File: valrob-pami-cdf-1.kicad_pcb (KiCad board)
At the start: 4 copper layers, 58 x 50 mm, 138 parts, among them J1 Conn_01x04, J2 USB_C_Receptacle_USB2.0_14P, J3 Conn_01x02, J4 Conn_01x04_Pin, J5 Conn_01x06, M1 Motor_Servo, M2 Stepper_Motor_bipolar, M3 Stepper_Motor_bipolar, Q1 Q_NMOS, Q2 Q_NMOS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

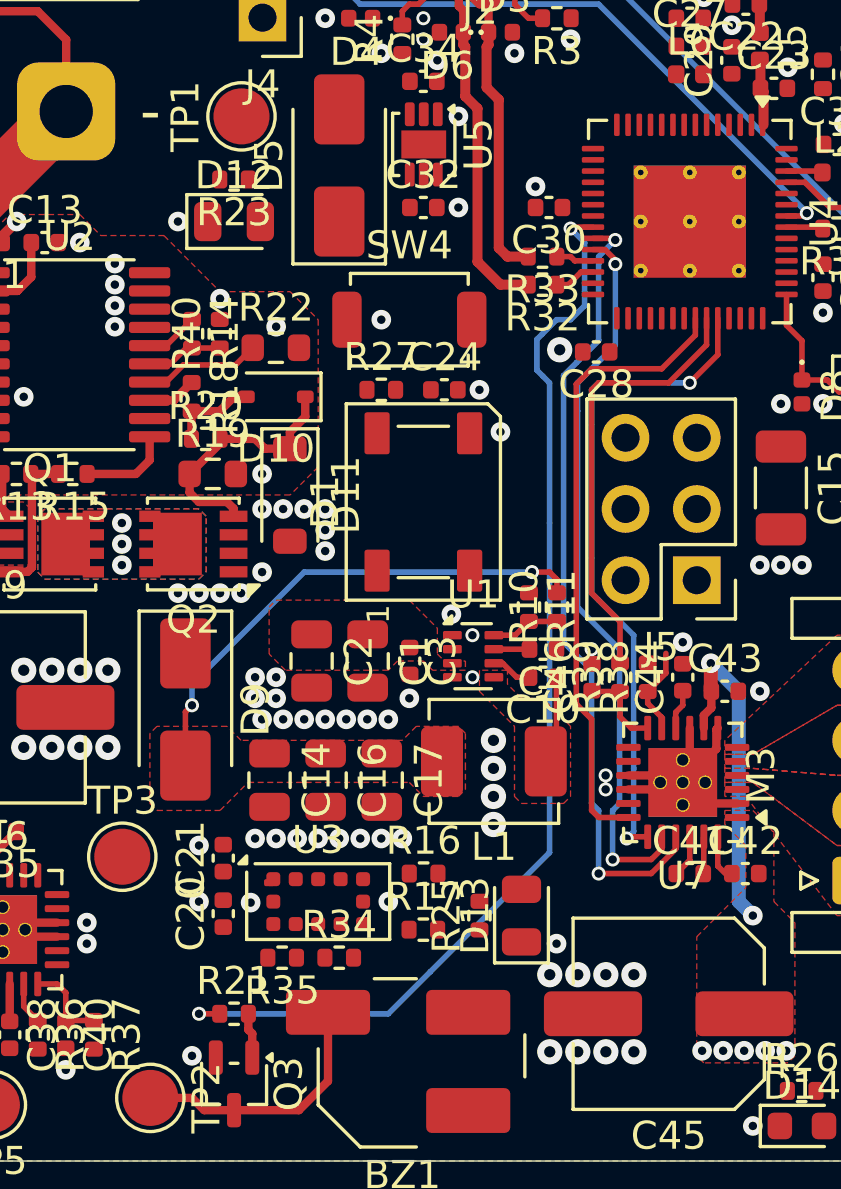
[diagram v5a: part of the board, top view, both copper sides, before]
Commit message: pcb: add tof sensor routing
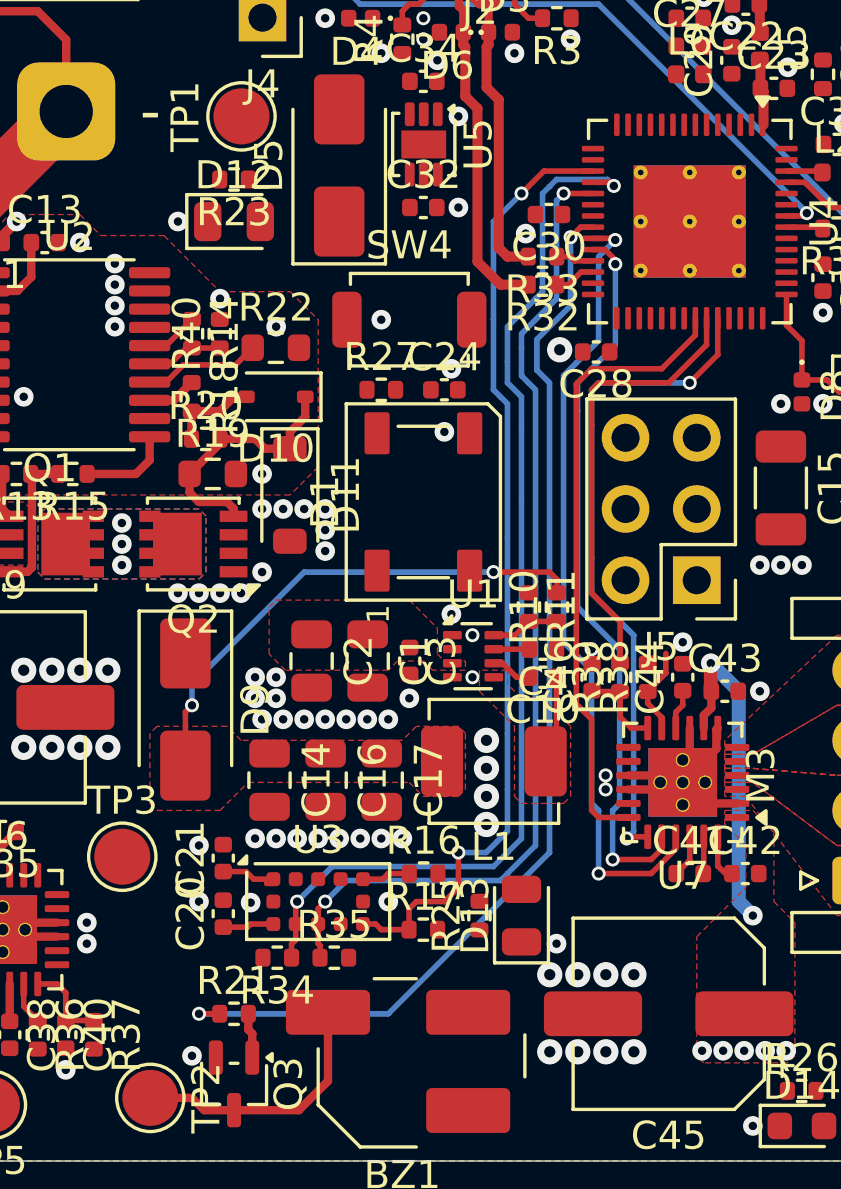
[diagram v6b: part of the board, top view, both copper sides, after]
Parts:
- moved R34 2.21 mm to (154.0, 115.8), turned to 180 degrees
- moved R35 1.86 mm to (156.1, 115.8), turned to 0 degrees
- moved C30 0.25 mm to (163.7, 89.2)
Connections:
- R17 pad 1: Net-(U3-GPIO1) -> /TOF_INT
- R34 pad 1: /SDA -> /SCL
- R34 pad 2: unconnected-(R34-Pad2) -> +3V3
- R35 pad 1: /SCL -> /SDA
- U3 pad 7: Net-(U3-GPIO1) -> /TOF_INT
- U4 pad 17: unconnected-(U4-GPIO12/ADC2_CH1-Pad17) -> /TOF_INT
- U4 pad 18: unconnected-(U4-GPIO13/ADC2_CH2-Pad18) -> /SCL
- U4 pad 19: unconnected-(U4-GPIO14/ADC2_CH3-Pad19) -> /SDA
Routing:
- net /SCL: track 0.00 -> 38.5 mm, vias 0 -> 2
- net /SDA: track 0.00 -> 35.6 mm, vias 0 -> 2
- net /TOF_INT: track 0.00 -> 34.1 mm, vias 0 -> 2
- net +3V3: track 0.00 -> 3.73 mm
- net Net-(U3-XSHUT): track 0.00 -> 1.73 mm
- net /BUZZER: track 40.1 -> 39.2 mm

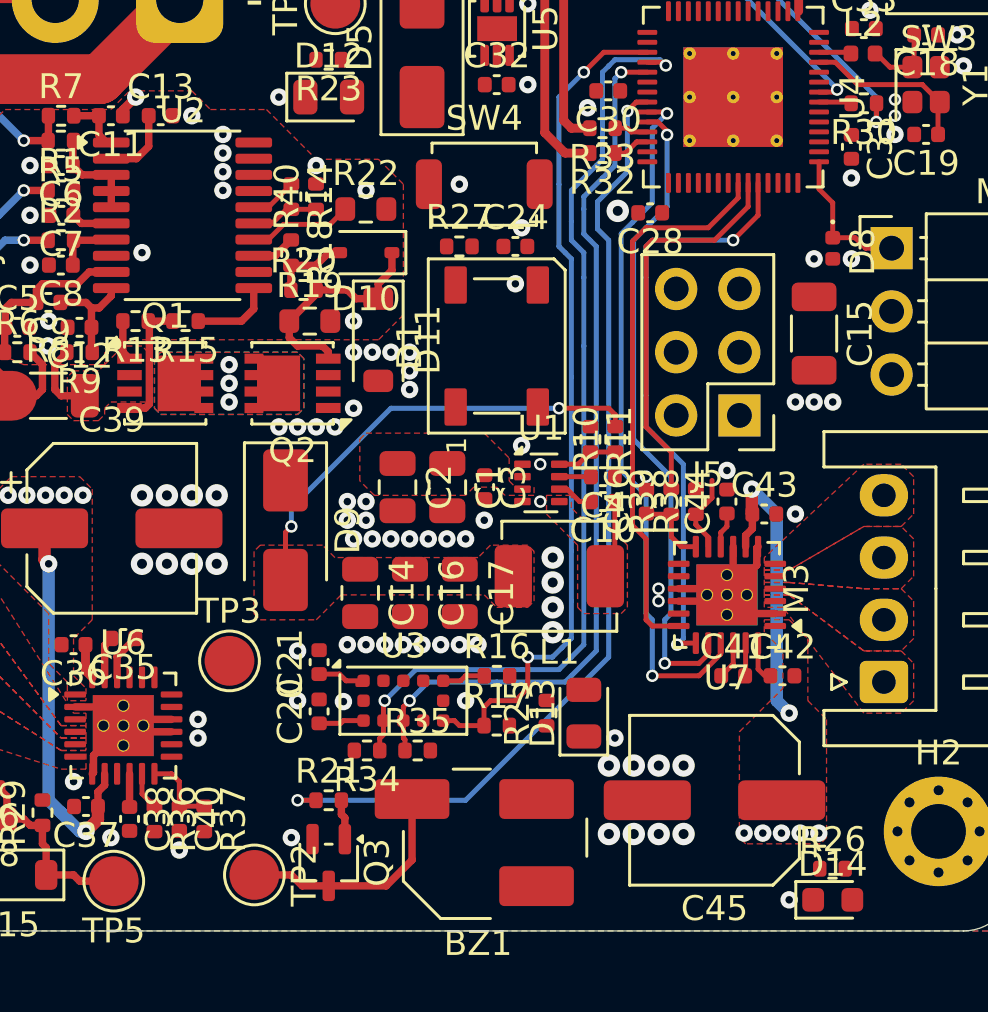
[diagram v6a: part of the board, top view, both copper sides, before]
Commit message: pcb: add missing stepper drv fault 2 connection
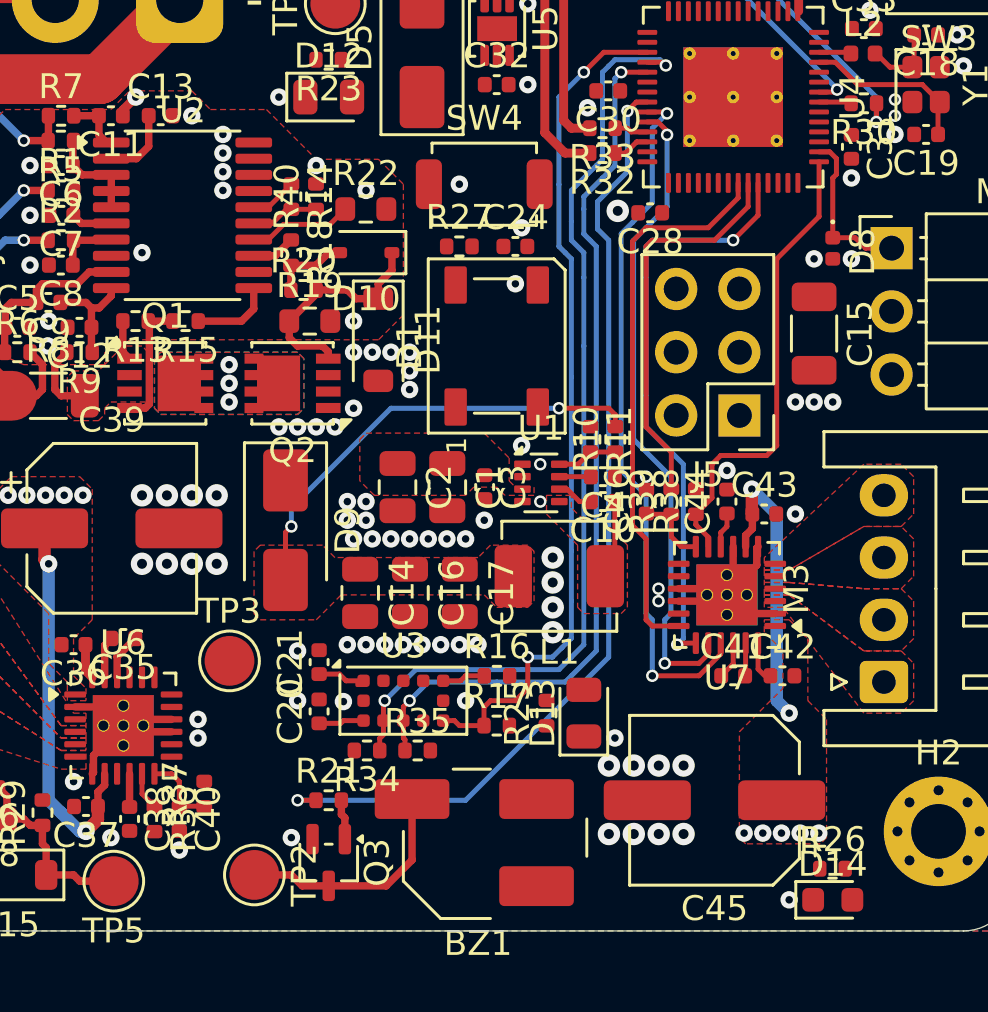
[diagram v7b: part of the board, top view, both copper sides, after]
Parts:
- moved R37 1.00 mm to (147.5, 117.5), turned to 90 degrees
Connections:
- U4 pad 43: /SERVO1 -> /~{FAULT_2}
- U4 pad 44: unconnected-(U4-MTCK/JTAG/GPIO39-Pad44) -> /SERVO1
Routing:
- net /~{FAULT_2}: track 3.14 -> 18.8 mm
- net /SERVO1: track 5.82 -> 6.59 mm

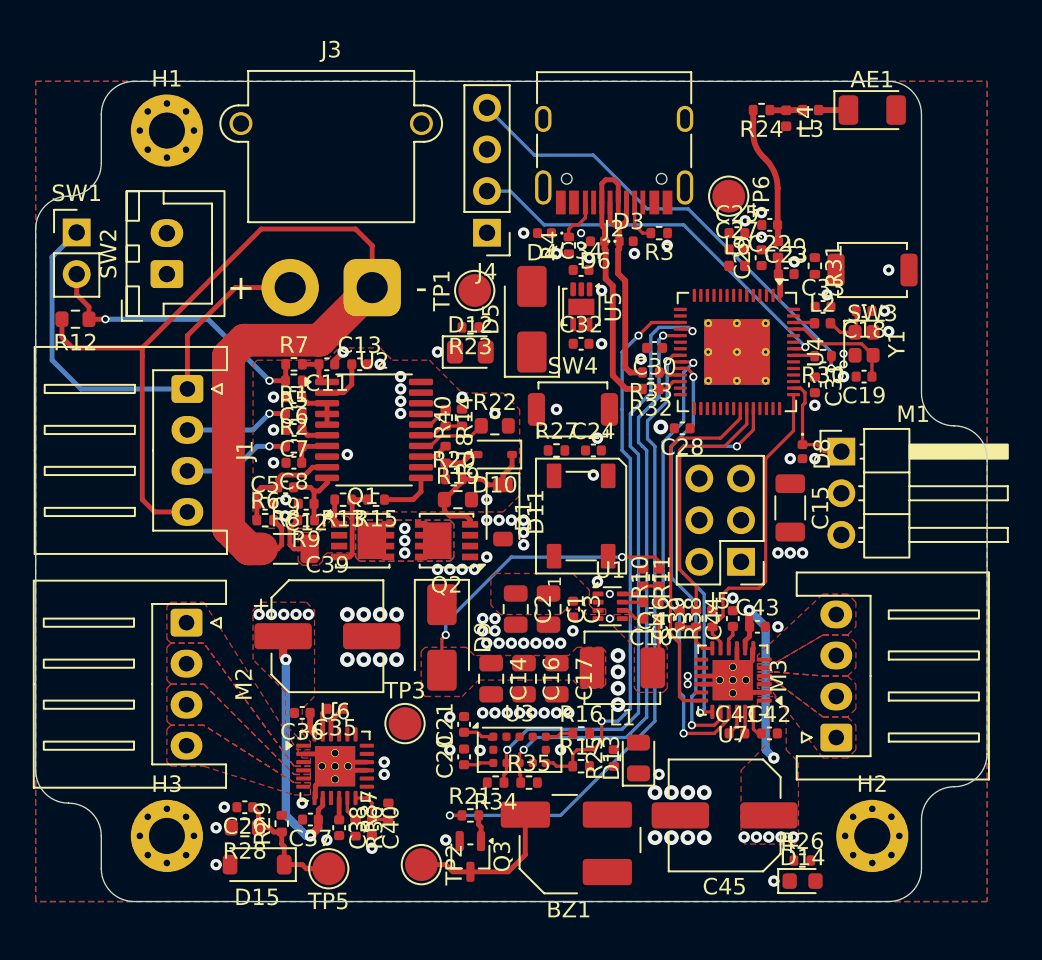
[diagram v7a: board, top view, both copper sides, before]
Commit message: pcb: add left stepper driver routing
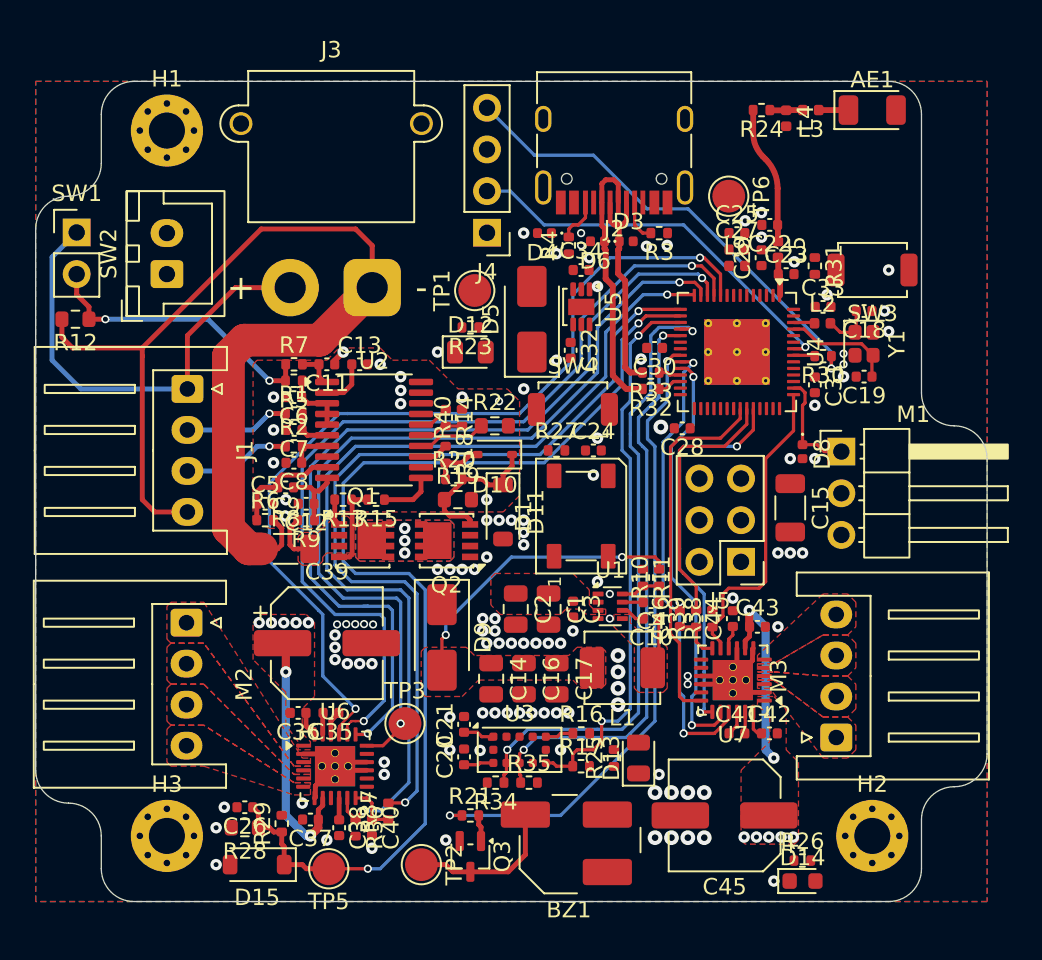
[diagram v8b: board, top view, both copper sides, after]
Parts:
- moved C32 0.75 mm to (158.6, 89.4), turned to -90 degrees
- moved C39 0.43 mm to (143.8, 107.2)
- moved C35 0.35 mm to (144.0, 111.5)
- moved C36 0.25 mm to (142.0, 111.5)
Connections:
- U4 pad 10: unconnected-(U4-GPIO5/ADC1_CH4-Pad10) -> /~{SLEEP_1}
- U4 pad 11: /~{FAULT_1} -> /EN_1
- U4 pad 12: /EMS -> /DIR_1
- U4 pad 13: /VPWM_1 -> /STEP_1
- U4 pad 14: unconnected-(U4-GPIO9/ADC1_CH8-Pad14) -> /~{FAULT_1}
- U4 pad 15: /Vsense -> /VPWM_1
- U4 pad 16: unconnected-(U4-GPIO11/ADC2_CH0-Pad16) -> /Vsense
- U4 pad 6: /DIR_1 -> unconnected-(U4-GPIO1/ADC1_CH0-Pad6)
- U4 pad 7: /STEP_1 -> /EMS
- U4 pad 8: /EN_1 -> unconnected-(U4-GPIO3/ADC1_CH2-Pad8)
- U4 pad 9: /~{SLEEP_1} -> unconnected-(U4-GPIO4/ADC1_CH3-Pad9)
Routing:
- net /Vsense: track 7.80 -> 65.9 mm, vias 0 -> 2
- net /~{FAULT_1}: track 1.51 -> 57.0 mm, vias 0 -> 2
- net /~{SLEEP_1}: track 0.00 -> 55.2 mm, vias 0 -> 2
- net /EN_1: track 0.00 -> 54.7 mm, vias 0 -> 2
- net /DIR_1: track 0.00 -> 53.4 mm, vias 0 -> 2
- net /STEP_1: track 0.00 -> 52.5 mm, vias 0 -> 2
- net /VPWM_1: track 0.00 -> 52.0 mm, vias 0 -> 2
- net GND: vias 108 -> 111
- net BGND: vias 13 -> 11
